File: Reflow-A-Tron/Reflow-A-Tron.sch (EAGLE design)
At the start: 38 parts, among them IC1 ATMEGA644-10PU, Q1 FOXSLF/200-20, Q2 BSS123, U2 MC7805, U4 MAX6675

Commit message: layout complete
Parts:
- added J2: HOT, neilbetham:8191
- added J3: NEUTRAL, neilbetham:8191
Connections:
- removed net N$16: D3.A2, R9.2
- removed net N$17: C11.1, D3.A1, R10.1
- removed net N$18: R11.2, R7.2
- removed net N$21: D4.C, Q2.D
- new net HOT: D3.A2, J2.1, R9.2
- new net NEUTRAL: C11.1, D3.A1, J3.1, R10.1
- net 5V: now also R11.2, R7.2
- net N$19: now also D4.C, Q2.D
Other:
- moved on the sheet: OK1
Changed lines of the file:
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@@
 <part name="R11" library="resistor" deviceset="R-US_" device="R0805" value="150"/>
 <part name="Q2" library="transistor-small-signal" deviceset="BSS123" device=""/>
+<part name="J2" library="neilbetham" deviceset="8191" device="" value="HOT"/>
+<part name="J3" library="neilbetham" deviceset="8191" device="" value="NEUTRAL"/>
 </parts>
 <sheets>
@@
 <instance part="GND4" gate="1" x="-58.42" y="53.34"/>
 <instance part="C6" gate="G$1" x="-58.42" y="33.02"/>
-<instance part="GND5" gate="1" x="-60.96" y="27.94"/>
-<instance part="SUPPLY6" gate="G$1" x="-60.96" y="38.1"/>
+<instance part="GND5" gate="1" x="-60.96" y="25.4"/>
+<instance part="SUPPLY6" gate="G$1" x="-60.96" y="40.64"/>
 <instance part="Q1" gate="G$1" x="-58.42" y="10.16"/>
 <instance part="C7" gate="G$1" x="-63.5" y="5.08"/>
@@
 <instance part="SUPPLY5" gate="G$1" x="165.1" y="5.08"/>
 <instance part="D3" gate="G$1" x="307.34" y="35.56" rot="MR0"/>
-<instance part="OK1" gate="G$1" x="218.44" y="35.56"/>
+<instance part="OK1" gate="G$1" x="220.98" y="35.56"/>
 <instance part="GND9" gate="1" x="198.12" y="7.62"/>
 <instance part="R8" gate="G$1" x="251.46" y="48.26"/>
@@
 <instance part="C11" gate="G$1" x="264.16" y="22.86"/>
 <instance part="R7" gate="G$1" x="203.2" y="45.72" rot="R90"/>
-<instance part="SUPPLY10" gate="G$1" x="198.12" y="53.34"/>
+<instance part="SUPPLY10" gate="G$1" x="198.12" y="55.88"/>
 <instance part="D4" gate="G$1" x="193.04" y="35.56"/>
 <instance part="R11" gate="G$1" x="193.04" y="45.72" rot="R90"/>
 <instance part="Q2" gate="G$1" x="198.12" y="17.78"/>
+<instance part="J2" gate="G$1" x="322.58" y="48.26"/>
+<instance part="J3" gate="G$1" x="322.58" y="15.24"/>
 </instances>
 <busses>
@@
 <wire x1="165.1" y1="-2.54" x2="165.1" y2="5.08" width="0.1524" layer="91"/>
 <pinref part="SUPPLY5" gate="G$1" pin="5V"/>
+</segment>
+<segment>
+<pinref part="R11" gate="G$1" pin="2"/>
+<wire x1="193.04" y1="53.34" x2="193.04" y2="50.8" width="0.1524" layer="91"/>
+<pinref part="R7" gate="G$1" pin="2"/>
+<wire x1="203.2" y1="53.34" x2="203.2" y2="50.8" width="0.1524" layer="91"/>
+<wire x1="193.04" y1="53.34" x2="198.12" y2="53.34" width="0.1524" layer="91"/>
+<pinref part="SUPPLY10" gate="G$1" pin="5V"/>
+<wire x1="198.12" y1="53.34" x2="203.2" y2="53.34" width="0.1524" layer="91"/>
+<wire x1="198.12" y1="55.88" x2="198.12" y2="53.34" width="0.1524" layer="91"/>
+</segment>
+<segment>
+<pinref part="SUPPLY6" gate="G$1" pin="5V"/>
+<wire x1="-60.96" y1="40.64" x2="-60.96" y2="38.1" width="0.1524" layer="91"/>
+<wire x1="-60.96" y1="38.1" x2="-58.42" y2="38.1" width="0.1524" layer="91"/>
 </segment>
 </net>
@@
 <segment>
 <pinref part="C6" gate="G$1" pin="1"/>
-<wire x1="-58.42" y1="38.1" x2="-60.96" y2="38.1" width="0.1524" layer="91"/>
 <wire x1="-58.42" y1="38.1" x2="-48.26" y2="38.1" width="0.1524" layer="91"/>
-<pinref part="SUPPLY6" gate="G$1" pin="5V"/>
 <label x="-48.26" y="38.1" size="1.778" layer="95"/>
 </segment>
@@
 </net>
 <net name="GND-MCU" class="0">
-<segment>
-<pinref part="GND5" gate="1" pin="GND"/>
-<pinref part="C6" gate="G$1" pin="2"/>
-<wire x1="-60.96" y1="30.48" x2="-58.42" y2="30.48" width="0.1524" layer="91"/>
-<wire x1="-58.42" y1="30.48" x2="-48.26" y2="30.48" width="0.1524" layer="91"/>
-<label x="-48.26" y="30.48" size="1.778" layer="95"/>
-</segment>
 <segment>
 <pinref part="IC1" gate="G$1" pin="GND"/>
@@
 <label x="-63.5" y="-5.08" size="1.778" layer="95"/>
 <junction x="-63.5" y="-2.54"/>
+</segment>
+<segment>
+<pinref part="C6" gate="G$1" pin="2"/>
+<wire x1="-58.42" y1="30.48" x2="-48.26" y2="30.48" width="0.1524" layer="91"/>
+<label x="-48.26" y="30.48" size="1.778" layer="95"/>
+<pinref part="GND5" gate="1" pin="GND"/>
+<wire x1="-58.42" y1="30.48" x2="-60.96" y2="30.48" width="0.1524" layer="91"/>
+<wire x1="-60.96" y1="30.48" x2="-60.96" y2="27.94" width="0.1524" layer="91"/>
 </segment>
 </net>
@@
 <segment>
 <pinref part="OK1" gate="G$1" pin="A"/>
-<wire x1="203.2" y1="38.1" x2="208.28" y2="38.1" width="0.1524" layer="91"/>
+<wire x1="203.2" y1="38.1" x2="210.82" y2="38.1" width="0.1524" layer="91"/>
 <wire x1="203.2" y1="38.1" x2="203.2" y2="40.64" width="0.1524" layer="91"/>
 <pinref part="R7" gate="G$1" pin="1"/>
@@
 <wire x1="238.76" y1="48.26" x2="238.76" y2="38.1" width="0.1524" layer="91"/>
 <pinref part="OK1" gate="G$1" pin="A2"/>
-<wire x1="238.76" y1="38.1" x2="228.6" y2="38.1" width="0.1524" layer="91"/>
+<wire x1="238.76" y1="38.1" x2="231.14" y2="38.1" width="0.1524" layer="91"/>
 </segment>
 </net>
@@
 <segment>
 <pinref part="OK1" gate="G$1" pin="A1"/>
-<wire x1="228.6" y1="33.02" x2="287.02" y2="33.02" width="0.1524" layer="91"/>
+<wire x1="231.14" y1="33.02" x2="287.02" y2="33.02" width="0.1524" layer="91"/>
 <pinref part="D3" gate="G$1" pin="G"/>
 <pinref part="R10" gate="G$1" pin="2"/>
@@
 </segment>
 </net>
-<net name="N$16" class="0">
+<net name="HOT" class="0">
 <segment>
 <pinref part="R9" gate="G$1" pin="2"/>
 <wire x1="284.48" y1="48.26" x2="307.34" y2="48.26" width="0.1524" layer="91"/>
 <pinref part="D3" gate="G$1" pin="A2"/>
-<wire x1="307.34" y1="48.26" x2="340.36" y2="48.26" width="0.1524" layer="91"/>
+<wire x1="307.34" y1="48.26" x2="314.96" y2="48.26" width="0.1524" layer="91"/>
 <wire x1="307.34" y1="43.18" x2="307.34" y2="48.26" width="0.1524" layer="91"/>
-</segment>
-</net>
-<net name="N$17" class="0">
+<pinref part="J2" gate="G$1" pin="1"/>
+<label x="309.88" y="50.8" size="1.778" layer="95"/>
+</segment>
+</net>
+<net name="NEUTRAL" class="0">
 <segment>
 <pinref part="C11" gate="G$1" pin="1"/>
@@
 <pinref part="R10" gate="G$1" pin="1"/>
 <wire x1="287.02" y1="15.24" x2="307.34" y2="15.24" width="0.1524" layer="91"/>
-<wire x1="307.34" y1="15.24" x2="340.36" y2="15.24" width="0.1524" layer="91"/>
+<wire x1="307.34" y1="15.24" x2="314.96" y2="15.24" width="0.1524" layer="91"/>
 <wire x1="287.02" y1="17.78" x2="287.02" y2="15.24" width="0.1524" layer="91"/>
 <pinref part="D3" gate="G$1" pin="A1"/>
@@
 <junction x="287.02" y="15.24"/>
 <junction x="307.34" y="15.24"/>
+<pinref part="J3" gate="G$1" pin="1"/>
+<label x="302.26" y="10.16" size="1.778" layer="95"/>
 </segment>
 </net>
@@
 </segment>
 </net>
-<net name="N$18" class="0">
-<segment>
-<pinref part="SUPPLY10" gate="G$1" pin="5V"/>
-<pinref part="R11" gate="G$1" pin="2"/>
-<wire x1="198.12" y1="53.34" x2="193.04" y2="53.34" width="0.1524" layer="91"/>
-<wire x1="193.04" y1="53.34" x2="193.04" y2="50.8" width="0.1524" layer="91"/>
-<pinref part="R7" gate="G$1" pin="2"/>
-<wire x1="198.12" y1="53.34" x2="203.2" y2="53.34" width="0.1524" layer="91"/>
-<wire x1="203.2" y1="53.34" x2="203.2" y2="50.8" width="0.1524" layer="91"/>
-</segment>
-</net>
 <net name="N$20" class="0">
 <segment>
@@
 <segment>
 <pinref part="OK1" gate="G$1" pin="C"/>
-<wire x1="208.28" y1="33.02" x2="203.2" y2="33.02" width="0.1524" layer="91"/>
+<wire x1="210.82" y1="33.02" x2="203.2" y2="33.02" width="0.1524" layer="91"/>
 <wire x1="203.2" y1="25.4" x2="203.2" y2="33.02" width="0.1524" layer="91"/>
-</segment>
-</net>
-<net name="N$21" class="0">
-<segment>
 <pinref part="D4" gate="G$1" pin="C"/>
 <wire x1="193.04" y1="30.48" x2="193.04" y2="25.4" width="0.1524" layer="91"/>
 <wire x1="193.04" y1="25.4" x2="198.12" y2="25.4" width="0.1524" layer="91"/>
 <pinref part="Q2" gate="G$1" pin="D"/>
-<wire x1="198.12" y1="25.4" x2="203.2" y2="25.4" width="0.1524" layer="91"/>
 <wire x1="198.12" y1="25.4" x2="198.12" y2="22.86" width="0.1524" layer="91"/>
-</segment>
-</net>
+<wire x1="203.2" y1="25.4" x2="198.12" y2="25.4" width="0.1524" layer="91"/>
+</segment>
+</net>

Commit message: Name
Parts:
- U2: value MC7805 -> L4941BDT-TRDPAK-3; device neilbetham:MC7805 -> neilbetham:L4941BDT-TRDPAK-3
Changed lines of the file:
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@@
 <part name="SUPPLY3" library="SparkFun-Aesthetics" deviceset="VCC" device=""/>
 <part name="GND1" library="SparkFun-Aesthetics" deviceset="GND" device=""/>
-<part name="U2" library="neilbetham" deviceset="MC7805" device=""/>
+<part name="U2" library="neilbetham" deviceset="L4941BDT-TR" device="DPAK-3"/>
 <part name="C1" library="SparkFun-Capacitors" deviceset="10UF50V20%(1210)" device="" value="10uF"/>
 <part name="C2" library="SparkFun-Capacitors" deviceset="10UF50V20%(1210)" device="" value="10uF"/>

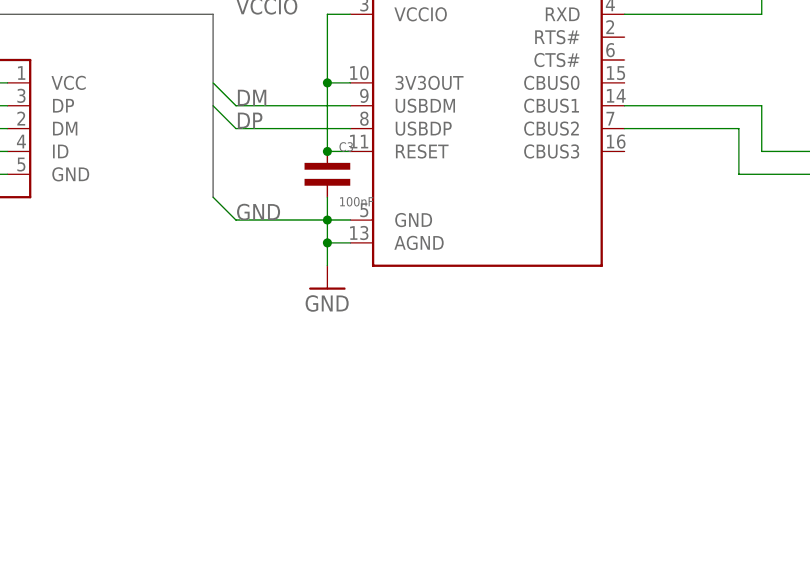
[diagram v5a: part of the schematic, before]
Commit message: Only keep relevant data sheets
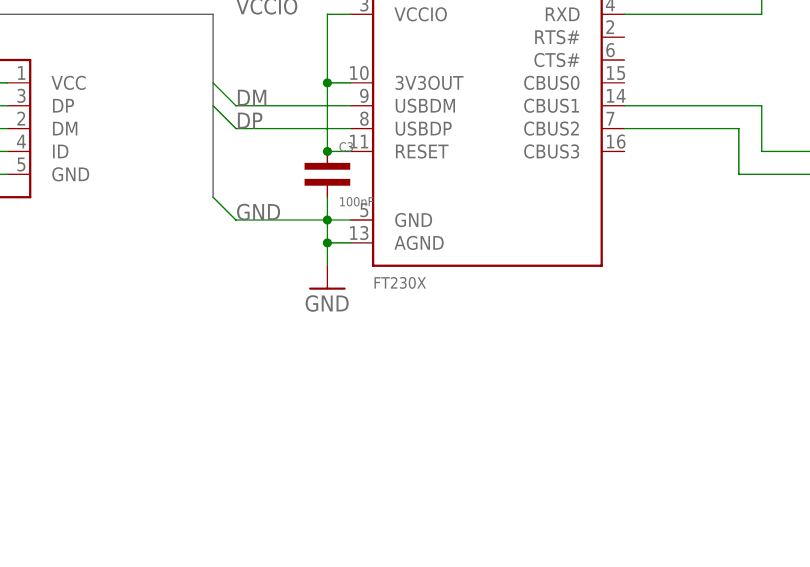
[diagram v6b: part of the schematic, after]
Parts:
- U1: value (none) -> FT230X
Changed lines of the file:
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@@
 <part name="SUPPLY7" library="SparkFun-Aesthetics" deviceset="VCC" device=""/>
 <part name="GND7" library="SparkFun-Aesthetics" deviceset="GND" device=""/>
-<part name="U1" library="neilbetham" deviceset="FT230X" device=""/>
+<part name="U1" library="neilbetham" deviceset="FT230X" device="" value="FT230X"/>
 <part name="J1" library="neilbetham" deviceset="XM7D-0512" device=""/>
 <part name="GND8" library="SparkFun-Aesthetics" deviceset="GND" device=""/>
